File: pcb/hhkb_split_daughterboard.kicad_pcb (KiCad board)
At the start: 2 copper layers, 21 x 32 mm, 5 parts

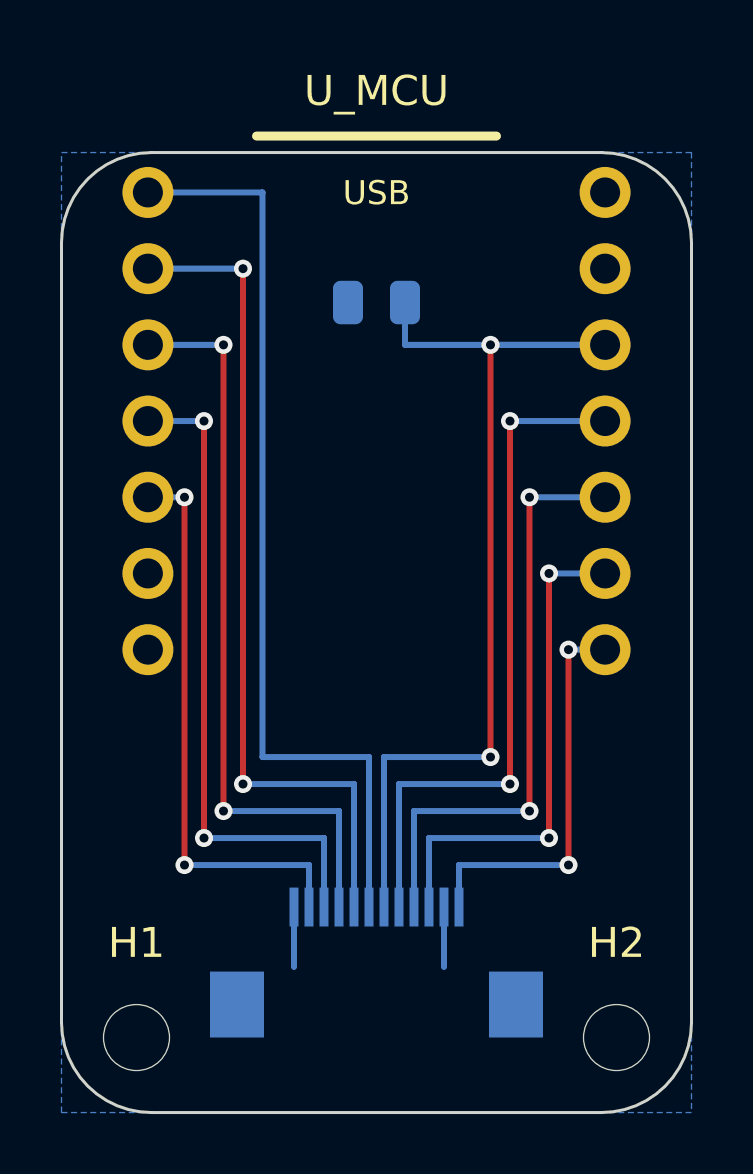
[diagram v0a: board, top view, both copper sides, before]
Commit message: バルクを子基板へ移し、電源鎖を消費側へ寄せ、行バスを直線にした
利用者の指摘を順に潰した。どれも「測ったら前提が違っていた」型。

1. バルク（C_BULK）を子基板へ
   守る相手は XIAO の µs 級の電流変動（electrical-design 1-5）で、
   595 でも整流点でもない。XIAO は子基板にいるので、主基板に置くと
   FFC 100mm のインダクタンスの外側から供給することになる。
   XIAO の 3V3 パッドから 2.04mm の位置へ移した。

2. 電源ブロックを V3V3 の消費側へ
   整流点 D_PWR が板の左端にあるのに、消費側（C_U1・U1・J_DB）は
   全部反対側だった。U1 の左へ寄せて V3V3 の銅 132→81mm、
   VBATT_SENSE 110→78mm。左の帯 0 はアンテナ禁止域と取付穴で
   分断されていて、プラス側へは出せない（一度出して DRC 13 件）。

3. 行のバスを裏面の直線で自分で引く（prewire_row_bus）
   ROW0 が 222mm・ビア 7 本・区間 54 で表裏を行き来していた。
   同じ行のダイオードの K 側は y が完全に一致し、ライン上に
   スルーホールが無いので直線が引ける（ROW4 は元から 0 ビアだった）。
   左の未配線 1 本（ROW2）はこれで解決した。
   ⚠️ DSN に (autoroute_settings) を足す道は駄目。左が 66 本に壊れた。

4. アンテナの禁止域（30x15mm）を削除
   利用者の「本当にアンテナの真上ですか」で測ったら、覆っていなかった。
     禁止域 y 30.60..45.60 / 基板後端 48.70 / アンテナ 49.50..53.00
   アンテナは基板の後端より 0.80mm 奥（XIAO_OVERHANG 1.8mm の効果）で、
   平面的に基板の外。禁止域は 3.9mm 的を外したまま 450mm² を捨て、
   左の配線を圧迫していた。
   **根拠に挙げられていた検査は存在しなかった。**interface.py は
   test_the_antenna_keepout_actually_covers_the_antenna が照合すると
   書いていたが、その名前の検査はどこにも無い。実在したのは
   「禁止域の中が空か」だけで、位置は誰も見ていなかった。
   代わりに test_the_antenna_clears_the_main_board を置いた
   （XIAO_OVERHANG を 0 にすると落ちることを確認済み）。

   → open-gaps #23 の幾何の証明（アンテナは必ず 4mm 以上 基板の下に
     入る）は、もう成立していない。ただし余裕は 0.80mm しかないので、
     手 0（アルミ箔で RSSI）の価値は残る。#23 の書き直しは次。

残っているもの（次に着手する）:
  右 未配線 3（GND 離島 1 + V3V3 が J_DB へ届かない 2）★機能的な故障
  左 未配線 1（GND 離島）
  違反はどれも 0。自前配線で塞ぐ案は取らない——今は綺麗に引けても
  配置を変えると黙って壊れ、再現性が無い（利用者の判断）。

pytest tools は未実行。

Co-Authored-By: Claude Opus 5 (1M context) <noreply@anthropic.com>
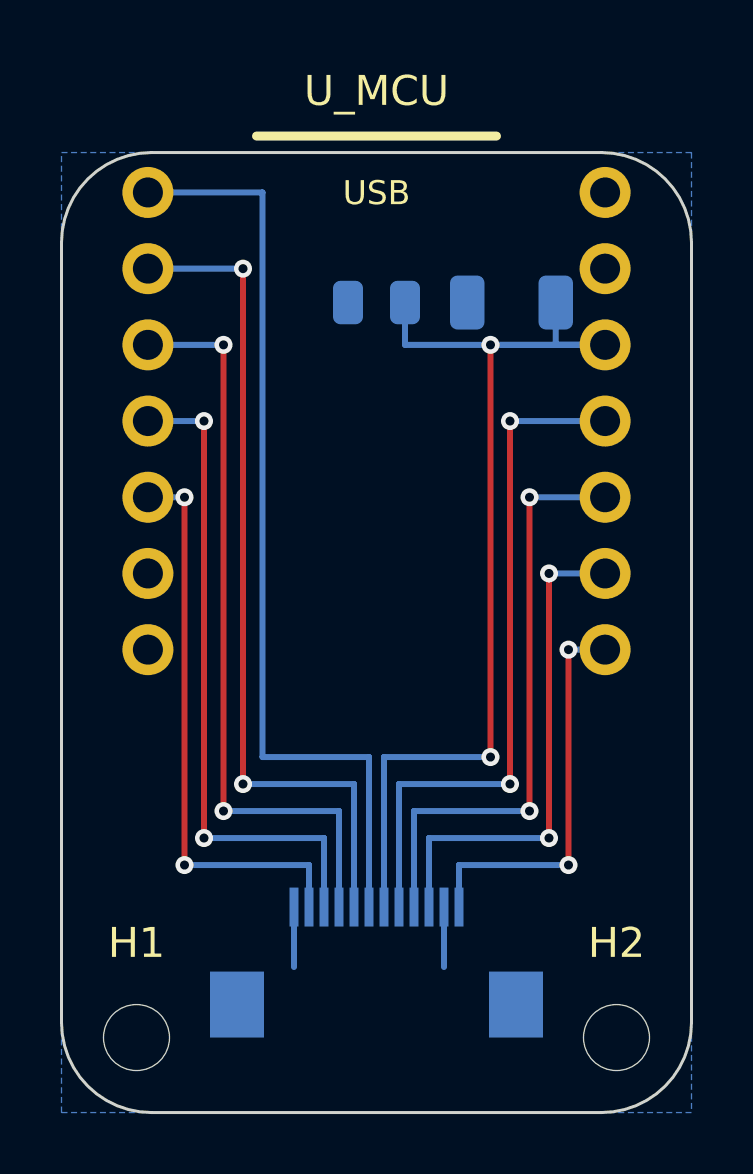
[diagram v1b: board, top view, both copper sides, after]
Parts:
- added C_BULK: 100uF, C_1206_3216Metric, B.Cu at (154.5, 89.0)
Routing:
- net V3V3: track 34.2 -> 37.2 mm

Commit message: 電源を子基板へ移し、FFC のピン順を両基板の都合から決め直した
利用者が絵を見ながら出した指摘を順に潰した回。**私は数字だけ見て
絵を見ておらず、同じ型の見落としを何度も拾ってもらった。**

■ 電源部を子基板へ（open-gaps #41）

  消費者は XIAO で、それは子基板にいる。起動と BLE 初期化で
  2.0〜2.5mA を継続、送信で 10〜15mA のパルス（task-c4-c5 測定 C /
  electrical-design 1-5）。595 の走査 100µA とは 100 倍以上ちがう。
  主基板で整流すると、その mA 級が FFC の 0.2mm 1 本を 100mm 渡る。

    FFC の V3V3   2.0〜2.5mA 継続 + パルス → **約 100µA**（150 分の 1）
    VBATT_SENSE   500kΩ が 100mm 渡る     → **渡らない**（ADC の 2mm 隣）
    ショットキー  隔離点まで FFC 100mm     → **3V3 パッド直近**
    主基板の帯    電源 5 点が SPI を塞ぐ   → **空いた**

  電池もスイッチも子基板のすぐ隣（実測: スイッチ→縁 左 4.0 / 右 20.7mm）
  なのでリード線はむしろ短くなる。

■ FFC のピン順（利用者「DB 単体でなく MAIN の都合も視野に入れて」）

  ROW0/1 は J_DB より上、ROW2/3/4 は下へ伸びる。行番号の昇順に並べると
  上下 2 群が必ず交差する（**実測 3 交差**）。群ごとに近い順で **0 交差**。
  そのズレは **XIAO のピン割り当て＝ファームで吸収**する（利用者の判断
  「配線でひねるのではなくソフトで受けるべき」）。

  ROW4 を D9 から左列へ戻した。右列へ逃がしていた理由は「左列が 6 本だと
  アンテナ直下を 2 本通る」だが、**その 6 本目は VBATT_SENSE だった。**
  分圧が子基板へ移って 5 本に戻ったので前提が消えた。
  → ファームの `&spi2_default`（MISO 外し）が**不要になり削除**。

■ アンテナの禁止域（利用者「こんなに広い必要ある？」「ズレてる」）

  子基板: 幅 18.3mm（XIAO の外形）を使っていた。**アンテナは 3.5mm 角**で
  4.1 倍。さらに y 方向に 2 つの細工（意味の無い切り詰めと水増し）があり、
  **アンテナの 57% しか覆っていなかった**。
    → `antenna_x_band()` に統一。**被覆 100%**、地板の無駄も消えた。
  主基板: アンテナから 3.9mm 外れた場所を抜いて 450mm² を捨てていた。
    → 削除（前のコミット）。

  ⚠️ **SES 往復でルール領域の層が消える**ことを発見した（GetLayer() が -1）。
  層を持たないゾーンは何も禁止しないので、あとから敷いたベタが
  アンテナ直下に入っていた（実測 3297 頂点）。`_restore_rule_area_layers`
  で戻す。**「宣言したから効いている」の 3 回目。**

■ 子基板を主基板と同じ水準に（利用者「MAIN にあって DB に無いもの」）

  両面 GND ベタ（裏面だけだった）・GND ファンアウト・スティッチング・
  離島の救済・電源のネットクラス。順序は **配置 → ネットクラス → 配線 →
  ベタ・ビア**（利用者「ベタは配線の残りで最大限やる」）。
  アンテナの禁止域だけは最初（配置と配線の制約なので）。

■ その他

  - バルクを縦置き＋向きを直した（V3V3/GND が XIAO と平行に並ぶ）
  - 行を D2〜D6 にして D1 を空け、奥側に 2.54mm 作った

■ 検査（どれも故意に壊して落ちることを確認）

  - `test_the_row_order_matches_between_firmware_and_circuit`
    行 N がファームと回路で同じピンを指すか。**既存の検査は集合しか
    見ておらず、D4 と D6 を入れ替えても通っていた**
  - 禁止域の寸法をアンテナの実寸と照合
  - `test_there_is_a_bulk_capacitor` を「XIAO と同じ基板にあるか」に
  - 変異検査が子基板も壊せるように（バルク移設で空振りしていた）
  - 正規表現がゾーンを跨いで**ベタ自身を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
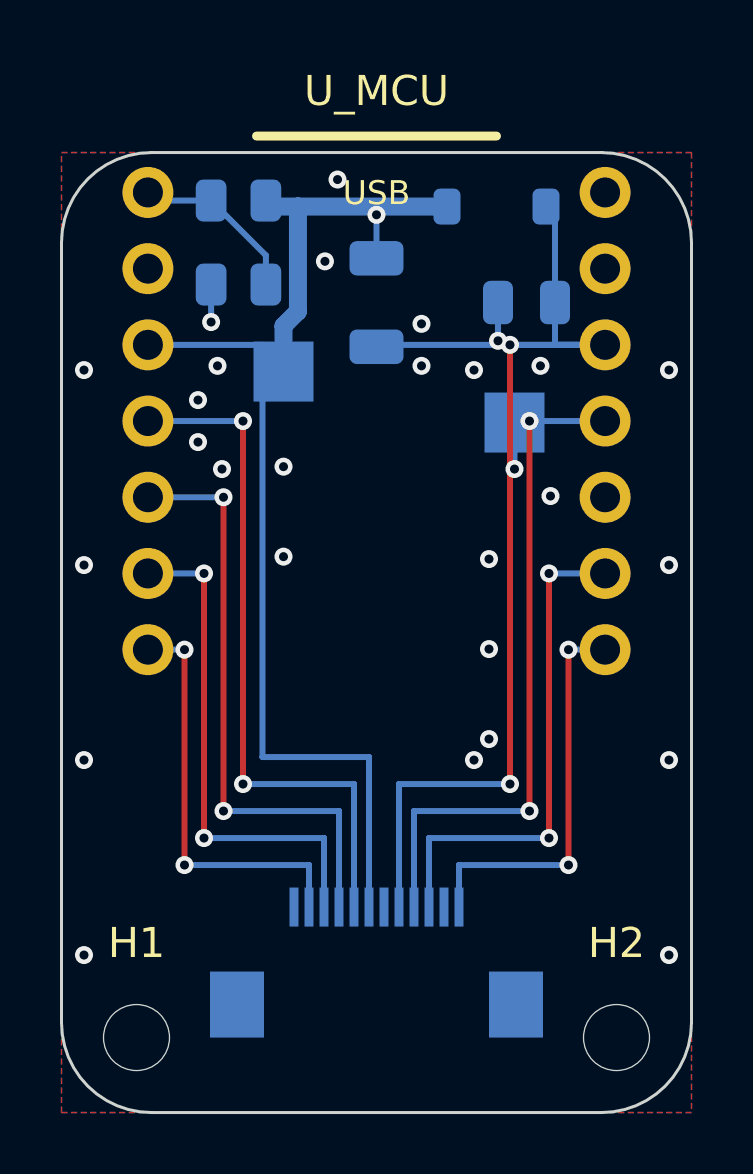
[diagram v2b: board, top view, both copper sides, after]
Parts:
- added BT1_-: battery_holder, TestPoint_Pad_2.0x2.0mm, B.Cu at (154.6, 93.0)
- added D_PWR: schottky, D_SOD-123, B.Cu at (154.0, 85.8)
- added R_HI: res_1M, R_0805_2012Metric, B.Cu at (145.4, 85.6)
- added R_LO: res_1M, R_0805_2012Metric, B.Cu at (145.4, 88.4)
- added SW_PWR_1: wire_pads, TestPoint_Pad_2.0x2.0mm, B.Cu at (146.9, 91.3)
- moved C_DB 5.00 mm to (155.0, 89.0)
- moved C_BULK 4.50 mm to (150.0, 89.0), turned to 90 degrees
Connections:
- J_MAIN pad 10: ROW2 -> ROW3
- J_MAIN pad 11: ROW3 -> ROW2
- J_MAIN pad 4: ROW4 -> SPI_MOSI
- J_MAIN pad 5: SPI_MOSI -> V3V3
- J_MAIN pad 6: V3V3 -> (no net)
- J_MAIN pad 7: VBATT_SENSE -> ROW0
- J_MAIN pad 8: ROW0 -> ROW1
- J_MAIN pad 9: ROW1 -> ROW4
- U_MCU pad D1: ROW0 -> (no net)
- U_MCU pad D2: ROW1 -> ROW0
- U_MCU pad D3: ROW2 -> ROW1
- U_MCU pad D4: ROW3 -> ROW4
- U_MCU pad D5: (no net) -> ROW3
- U_MCU pad D6: (no net) -> ROW2
- U_MCU pad D9: ROW4 -> (no net)
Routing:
- net VBATT_SENSE: track 31.2 -> 5.78 mm
- net VBATT_SW: track 0.00 -> 11.8 mm
- net ROW2: track 22.1 -> 14.0 mm
- net V3V3: track 37.2 -> 39.7 mm
- net ROW3: track 19.0 -> 17.0 mm
- net ROW1: track 25.1 -> 23.1 mm
- net ROW0: track 28.2 -> 26.1 mm, vias 2 -> 0
- net GND: track 4.00 -> 5.53 mm, vias 0 -> 29
- net SPI_MOSI: track 23.1 -> 22.6 mm
- added copper zone on F.Cu, net GND

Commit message: 子基板の配線を外周へ逃がし、電源部の向きを流れに合わせた
利用者が絵で示した「電源は盤面の外周を使い、中央を空ける」という
方針を実装した回。**私は数字だけ追っていて、絵を見た利用者の指摘の
ほうが毎回早く核心に届いた。**

■ 外周レーン（利用者「両側 2 ピンぐらいは外側から回せるのでは」）

  XIAO のパッド列（±7.62）の外に **2.03mm** ある。ここへ 2 本/側を
  逃がし、内側レーンを 5 本 → 2 本に減らした。

  ⚠️ **刻みはビアの径で決まる。**最初 0.4mm（配線の幅）で 3 本置いて
  DRC 13 件。φ0.6 + クリアランス 0.2 = **0.80mm 必要**で 2 本/側が上限。

  ⚠️ **ビアを省いて裏面のまま走らせる案は駄目。**間隔 0.40mm で 3 本
  入る（外周に裏面部品は無い）が、**層の分離を失う**。内側レーンへ
  向かう横枝は B.Cu なので、外側も B.Cu だと必ず交差する（実測 12 件）。
  **ビアは無駄ではなく、層を分けるために要る。**

■ 真下パス（利用者「D6/D7 は横向きでなく下向きに伸ばせる」）

  FFC に最も近い 1 本は、パッド列の x のまま真下へ降ろす。
  レーンもビアも使わない。ROW2 18.9→16.8mm、CS 18.4→16.2mm。

  ⚠️ 条件を `|x| > 7.0` で書いて**全パッドが該当**し、20mm の配線が
  盤面を横断して DRC 38 件。正しくは「その列で FFC に最も近い 1 本」
  ＝ i == 0。

■ 部品の向き（利用者「バルクの向きが逆」「電源周りこんな感じで」）

  - C_BULK: 縦置き（x 方向 1.4mm 節約）＋ **+90°**。XIAO は 3V3 が
    手前(9.59)・GND が奥(12.13) なので、同じ並びにして平行に届かせる
  - R_LO: 180°。SENSE が R_HI 側（左）を向き、分圧の中点が隣り合う
  - SW_PWR: 中央の縦帯（x ±0.9）を空ける。GND スティッチングが使う

■ 配線長

  子基板の合計 218.5 → **205.1mm**

DRC: 左 違反3/未配線0 / 右 違反2/未配線0 / 子基板 違反6/未配線1
（主基板は**両方とも未配線 0**。子基板の 6 件は下記）
test_circuit・test_daughterboard・test_keyscan・test_schematic・
test_pinmap = 81 件通過。**pytest tools 全体は未実行。**

Co-Authored-By: Claude Opus 5 (1M context) <noreply@anthropic.com>
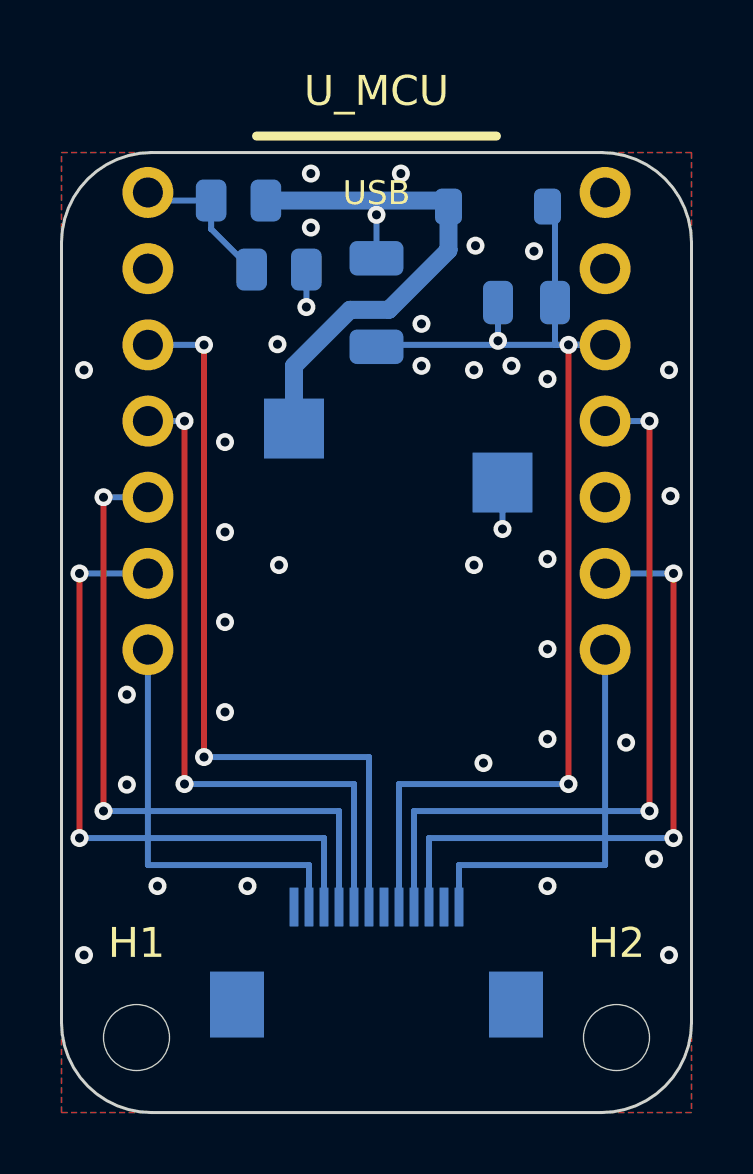
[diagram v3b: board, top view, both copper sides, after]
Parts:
- moved BT1_- 2.04 mm to (154.2, 95.0)
- moved SW_PWR_1 1.93 mm to (147.2, 93.2)
- moved R_LO 1.44 mm to (146.8, 87.9), turned to 0 degrees
- moved D_PWR 0.05 mm to (154.1, 85.8)
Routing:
- net VBATT_SW: track 11.8 -> 16.5 mm
- net SPI_SCK: track 17.0 -> 21.6 mm
- net ROW3: track 17.0 -> 21.6 mm
- net SPI_MOSI: track 22.6 -> 25.5 mm
- net ROW4: track 20.0 -> 23.0 mm
- net VBATT_SENSE: track 5.78 -> 5.08 mm
- net ROW2: vias 2 -> 0
- net ROW0: vias 0 -> 2
- net GND: vias 29 -> 37
- net CS: vias 2 -> 0

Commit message: 警告を数え、浮いた GND を辿って消し、FFC の地面を繋いだ
DRC の「違反 0」がエラーだけの数だった。--severity-error を外し、
警告を別の数として記録・表示する。左 35 / 右 48 / 子基板 24、
合計 107 件がそれまで構造的に見えなかった。合否はエラーだけで
決める（警告を混ぜると、MX フットプリントが持つ穴の間隔で
34 件が永久に赤になり、直せない赤が新しい赤を隠す）。

浮いた GND の判定が「区画の中にビアかパッドがあるか」だった。
それではビアの行き先を見ておらず、右基板では 23 区画すべてが
「浮いていない」と答えるのに DRC は未配線を報告していた。
ベタ・配線・ビアを同じ連結成分に載せ、本土へ辿り着けないものを
浮きとする。ベタだけ消すと配線とビアが残って宙に浮くので、
三者まとめて名指しで消す（面積の閾値では分けられない。浮きの
最大 3.01mm² が、繋がっている島の最小 1.51mm² より大きい）。

MAX_FLOATING_ISLANDS が同じファイルに 2 回定義されていて、
後の 12 が勝っていた。「0 でなければならない」と書いた検査が、
12 個まで黙って通していた。古い方を消す。

ELEC_REF に J_MAIN が無く、FFC の GND パッドにビアが打たれて
いなかった。J_DB だけあって対の J_MAIN が無い。対で書く。
主基板 2 枚に影響は無い（J_MAIN は子基板にしかない）。

穴を障害物に入れていなかった。パッドの外接箱は銅の広がりで、
NPTH の穴を表せない。要求される距離も違う（銅 0.2 対 穴 0.5）。
GND ビアがスイッチの穴に 0.479mm まで寄っていた。

子基板の V3V3 を FFC から電源群へ繋いだ。列の下へ降りて外へ
出てから上がる。降りる高さも外へ出る位置も、GND ビアと
取り付けパッドの実位置から計算する（固定値で書いて 3 度当てた）。

子基板 未配線 1 → 0。残る違反 1 件は gen_daughterboard が
gnd_fanout.place を呼ばず、Freerouting に渡す時点でビアが
存在しないため避けようがない件。順序の設計に関わるので別で扱う。

left / right の基板は再生成していない（今日のコード変更が
反映されていないので、記録だけ更新して現物は次回に回す）。

Co-Authored-By: Claude Opus 5 (1M context) <noreply@anthropic.com>
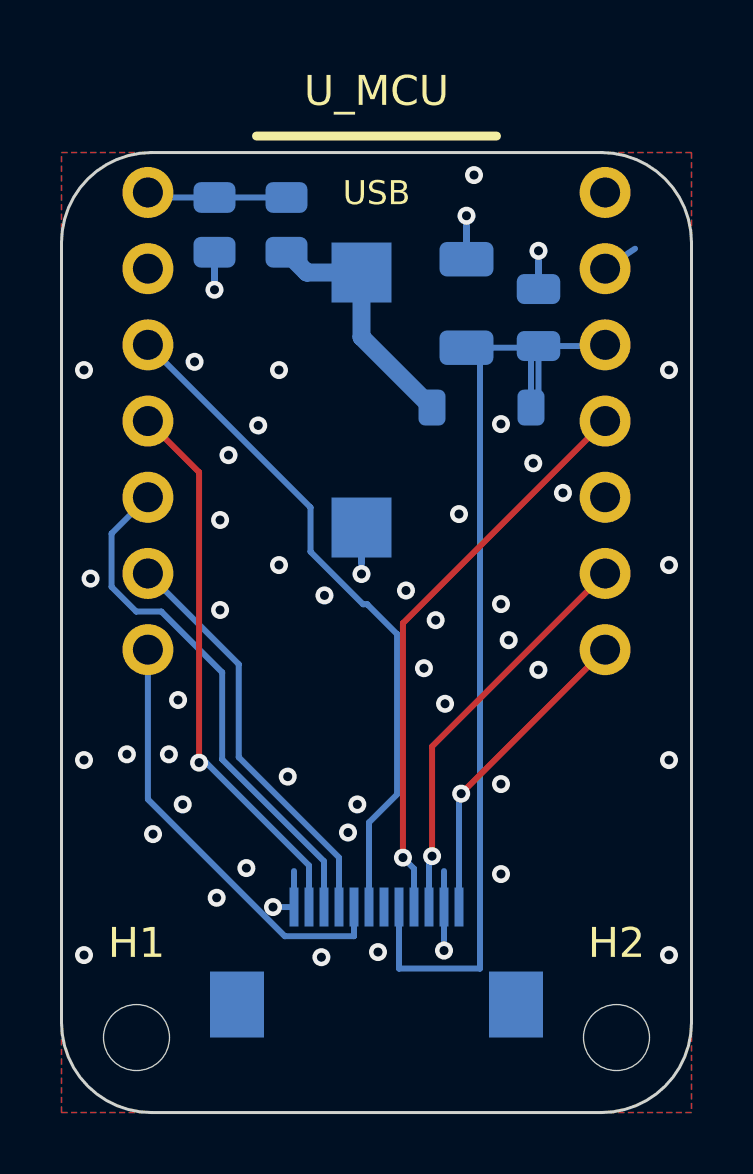
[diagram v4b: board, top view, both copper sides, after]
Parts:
- moved D_PWR 6.72 mm to (153.5, 92.5)
- moved SW_PWR_1 5.67 mm to (149.5, 88.0)
- moved BT1_- 4.93 mm to (149.5, 96.5)
- moved C_BULK 3.00 mm to (153.0, 89.0)
- moved R_LO 2.62 mm to (144.6, 86.4), turned to -90 degrees
- moved R_HI 1.79 mm to (147.0, 86.4), turned to 90 degrees
- moved C_DB 0.64 mm to (155.4, 89.5), turned to 90 degrees
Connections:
- U_MCU pad D3: ROW1 -> ROW2
- U_MCU pad D4: ROW4 -> ROW3
- U_MCU pad D5: ROW3 -> ROW4
- U_MCU pad D6: ROW2 -> ROW1
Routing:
- net GND: track 5.53 -> 16.1 mm, vias 37 -> 48
- net ROW4: track 23.0 -> 13.8 mm, vias 2 -> 0
- net ROW1: track 23.1 -> 14.7 mm, vias 2 -> 0
- net VBATT_SW: track 16.5 -> 8.25 mm
- net SPI_SCK: track 21.6 -> 13.6 mm, vias 2 -> 1
- net SPI_MOSI: track 25.5 -> 19.1 mm, vias 2 -> 1
- net V3V3: track 39.7 -> 34.6 mm, vias 2 -> 0
- net ROW2: track 14.0 -> 18.6 mm, vias 0 -> 1
- net ROW3: track 21.6 -> 17.6 mm, vias 2 -> 0
- net ROW0: track 26.1 -> 22.6 mm, vias 2 -> 0
- net CS: track 13.5 -> 10.6 mm, vias 0 -> 1

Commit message: 子基板の DRC を 0 にし、行を XIAO パッドの外周へ自分で引いた
**DRC のエラー 1 件は、子基板だけ GND ファンアウトを配線前に打って
いなかったのが原因だった。**主基板は gen_pcb が配置段階で
`gnd_fanout.place` を呼ぶのでビアが DSN に載り、Freerouting が避ける
（未配線の左 5 個・右 10 個）。**子基板は 0 個**だったのに、autoroute は
「配線前と同じ位置に戻るので衝突しない」と書いていた。前提が成立して
おらず、空き地と思って引かれた ROW1 の上にあとからビアが立っていた
（0.0091mm ＝ 実質短絡）。gen_daughterboard にも同じ一手を足した。

**ROW2/3/4 を XIAO のパッド列の外側へ、自分で引くようにした**（利用者
「D3〜D5 を外側に。D3 = ROW2 が最も外周側」）。

この並び自体は前からあったが、**絵に描いた餅だった。**配線後の基板を
実測すると列の外へ出ていたのは 2 本だけで、ROW3/ROW4 はパッド
（x=-7.62）で止まり、内側にいるはずの ROW0 が外周を取っていた。
自動配線器はこの計画を知らない。`_prewire_rows` で引いて実現した
（実測 x=-10.10/-9.70/-9.30・交差 0・斜め 0）。

**経路は L 字 3 回だけ。**一度は「上へ→左へ→下へ→左へ→上へ」と 5 回
折れていた（利用者「クネクネ迂回はやめて。最短で」）。中ほどの上下は
12 番 GND の引き出しが列の内側へ伸びていた頃の名残で、**その引き出しを
列の外側（下）へ向けた時点で不要になっていた。**消して 3 本の総長が
83.37 → **71.07mm**（各行とも外周経由の最短と一致）。

**シルクの参照名を 0.8mm に。**この基板だけ silk_overlap が 14 件あった
（主基板は 5〜6 件）。21mm 幅に電源部 5 個が固まり、8 文字の参照名が
隣に乗っていた。0.7mm は KiCad の text_height に触れるので 0.8 が下限。

    違反 1 → **0** / 未配線 0 / 警告 24 → **16**（すべてシルクの文字）

⚠️ **`PREWIRED_DB` に `ROW[234]` を足すのが対。**足さないと DSN に
未配線として残り、Freerouting が二重に引いて同じネットが自分自身と
交差する（2026-08-14 に手配線をやめた原因がこれだった）。SES 取り込みは
既存の配線を作り直すので、autoroute 側での立て直しも要る。

主基板の赤 6 件（bulk capacitor・net count・right の DRC）は**この変更の
前から**落ちている（変更を退避して確認済み）。子基板は 4 件とも通る。

Co-Authored-By: Claude Opus 5 (1M context) <noreply@anthropic.com>
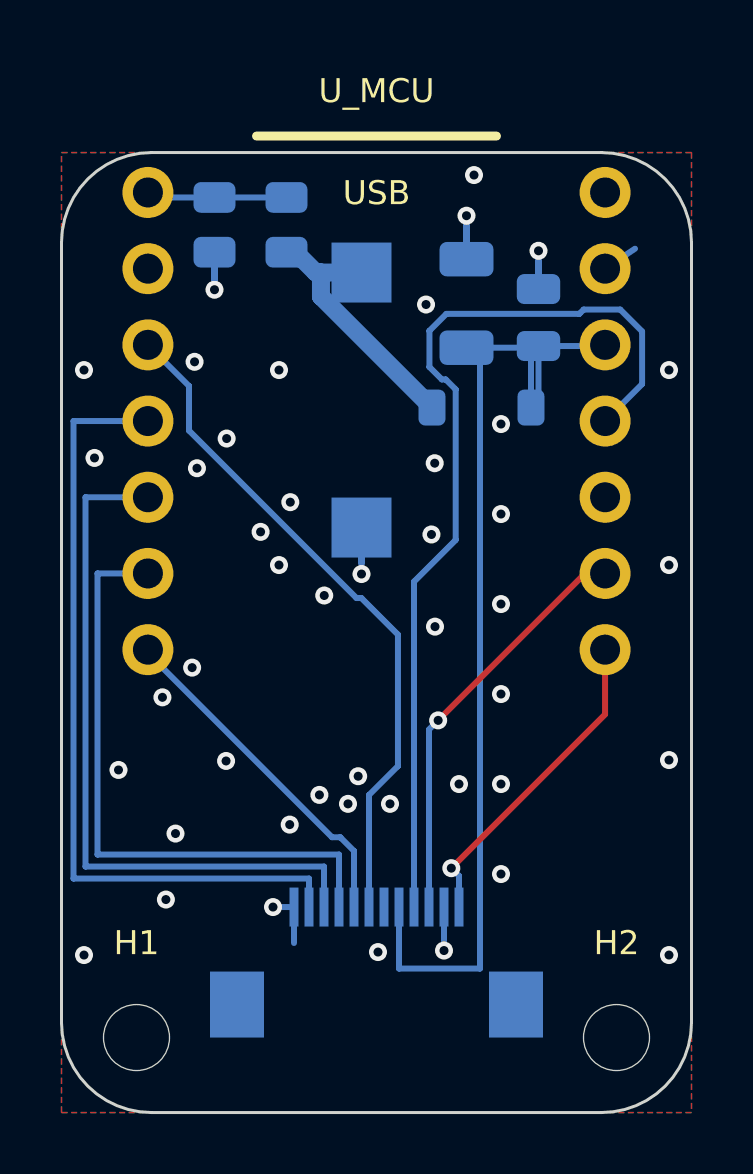
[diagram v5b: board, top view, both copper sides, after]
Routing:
- net SPI_MOSI: track 19.1 -> 31.4 mm, vias 1 -> 0
- net ROW2: track 18.6 -> 26.5 mm, vias 1 -> 0
- net ROW4: track 13.8 -> 20.9 mm
- net ROW3: track 17.6 -> 23.7 mm
- net ROW1: track 14.7 -> 11.6 mm
- net VBATT_SW: track 8.25 -> 8.81 mm
- net GND: vias 48 -> 45
